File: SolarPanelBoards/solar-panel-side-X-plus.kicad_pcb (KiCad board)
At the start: 2 copper layers, 82 x 99 mm, 24 parts, among them J1 Conn_01x06, U1 OPT3001DNPT

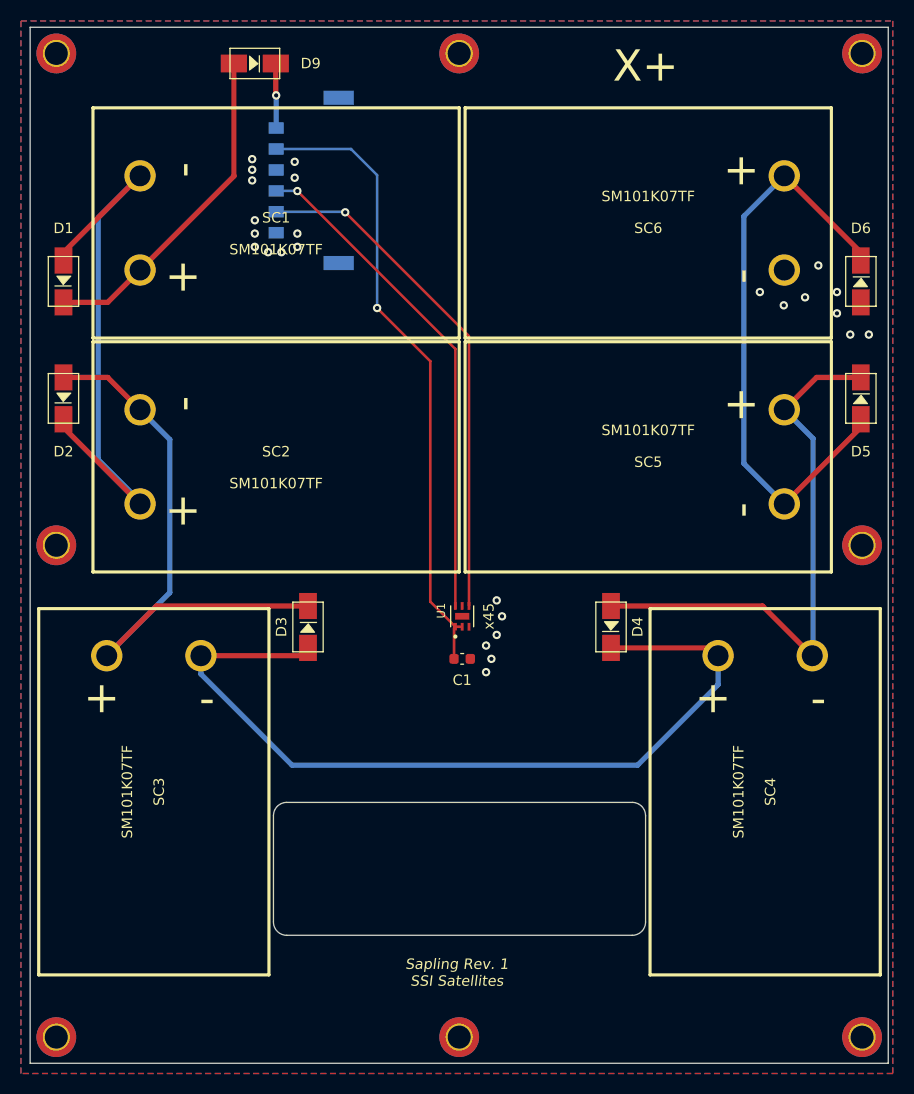
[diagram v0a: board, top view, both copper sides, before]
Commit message: Battery board and side panels ready for CAD check and review, pycubed not finished yet
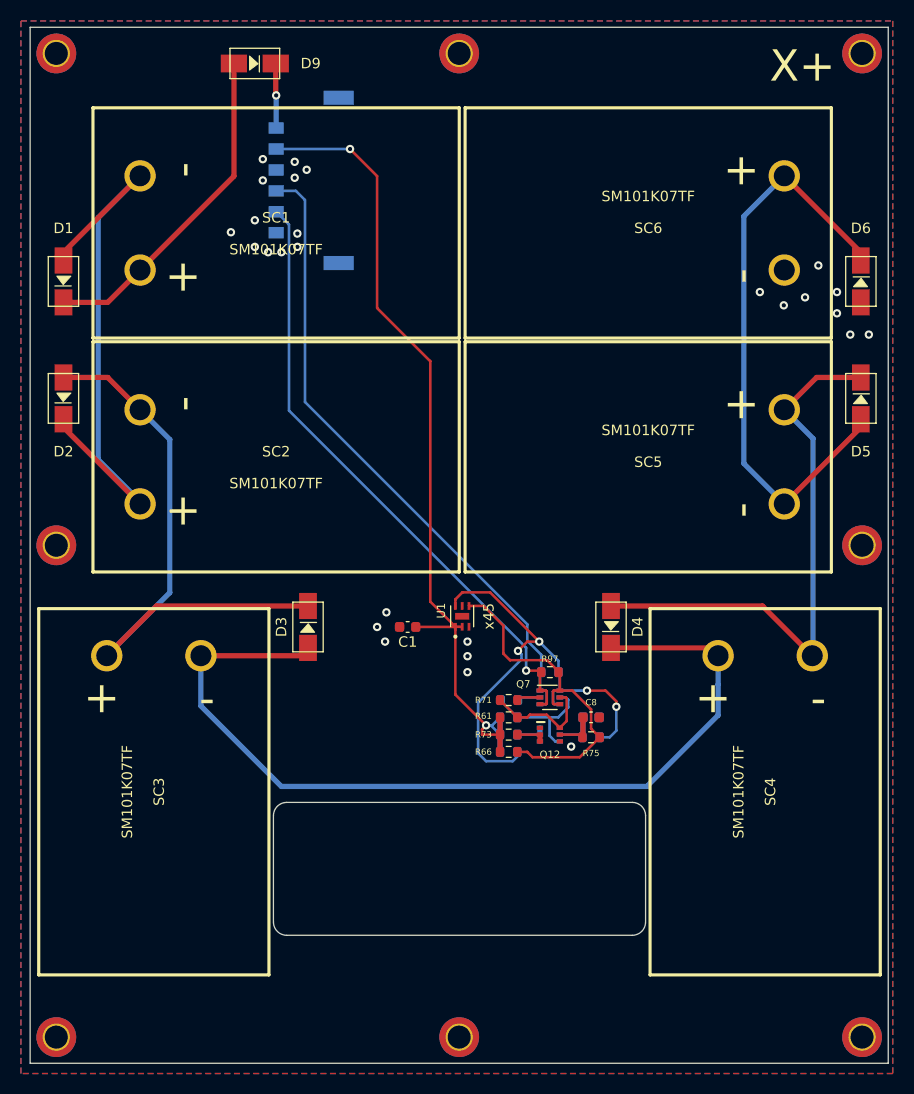
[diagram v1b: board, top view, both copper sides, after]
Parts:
- added C40: 10nF, Capacitor_SMD:C_0603_1608Metric, B.Cu at (151.0, 111.3)
- added C8: 10nF, Capacitor_SMD:C_0603_1608Metric, F.Cu at (151.0, 111.3)
- added Q12: BSS138DWQ-7, sapling:BSS138DWQ-7, F.Cu at (147.1, 112.9)
- added Q13: BSS138DWQ-7, sapling:BSS138DWQ-7, B.Cu at (147.1, 112.9)
- added Q7: MBT2222ADW1T1, Package_TO_SOT_SMD:SOT-363_SC-70-6, F.Cu at (147.1, 109.3)
- added Q8: MBT2222ADW1T1, Package_TO_SOT_SMD:SOT-363_SC-70-6, B.Cu at (147.1, 109.3)
- added R61: 10K, Resistor_SMD:R_0603_1608Metric, F.Cu at (143.1, 111.3)
- added R62: 10K, Resistor_SMD:R_0603_1608Metric, B.Cu at (143.1, 111.3)
- added R66: 10K, Resistor_SMD:R_0603_1608Metric, F.Cu at (143.1, 114.6)
- added R67: 10K, Resistor_SMD:R_0603_1608Metric, B.Cu at (143.1, 114.6)
- added R71: 680, Resistor_SMD:R_0603_1608Metric, F.Cu at (143.1, 109.6)
- added R72: 680, Resistor_SMD:R_0603_1608Metric, B.Cu at (143.2, 109.6)
- added R73: 100K, Resistor_SMD:R_0603_1608Metric, F.Cu at (143.1, 112.9)
- added R74: 100K, Resistor_SMD:R_0603_1608Metric, B.Cu at (143.1, 112.9)
- added R75: 200K, Resistor_SMD:R_0603_1608Metric, F.Cu at (151.0, 113.2)
- added R76: 200K, Resistor_SMD:R_0603_1608Metric, B.Cu at (151.0, 113.2)
- added R97: 0, Resistor_SMD:R_0603_1608Metric, F.Cu at (147.1, 106.9)
- added R98: 0, Resistor_SMD:R_0603_1608Metric, B.Cu at (147.1, 106.9)
- moved C1 6.03 mm to (133.5, 102.6), turned to 180 degrees
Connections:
- U1 pad 4: SCL -> SCL_SUN
- U1 pad 6: SDA -> SDA_SUN
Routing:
- net SDA_SUN: track 0.00 -> 48.0 mm, vias 0 -> 4
- net SCL_SUN: track 0.00 -> 32.7 mm
- net +3V3: track 60.7 -> 84.8 mm, vias 1 -> 2
- net SDA: track 47.9 -> 61.9 mm, vias 1 -> 0
- net Net-(Q13-Pad6): track 0.00 -> 12.2 mm
- net Net-(Q12-Pad6): track 0.00 -> 10.8 mm
- net SCL: track 49.1 -> 59.6 mm
- net Net-(D3-Pad2): track 81.8 -> 87.0 mm
- net Net-(C8-Pad1): track 0.00 -> 4.19 mm
- net Net-(C40-Pad1): track 0.00 -> 4.19 mm
- net Net-(Q13-Pad2): track 0.00 -> 2.81 mm
- net Net-(Q12-Pad2): track 0.00 -> 2.81 mm
- net Net-(Q7-Pad2): track 0.00 -> 2.27 mm
- net Net-(Q8-Pad2): track 0.00 -> 2.20 mm
- net GND: vias 26 -> 27
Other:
- board text removed: "Sapling Rev. 1 SSI Satellites"

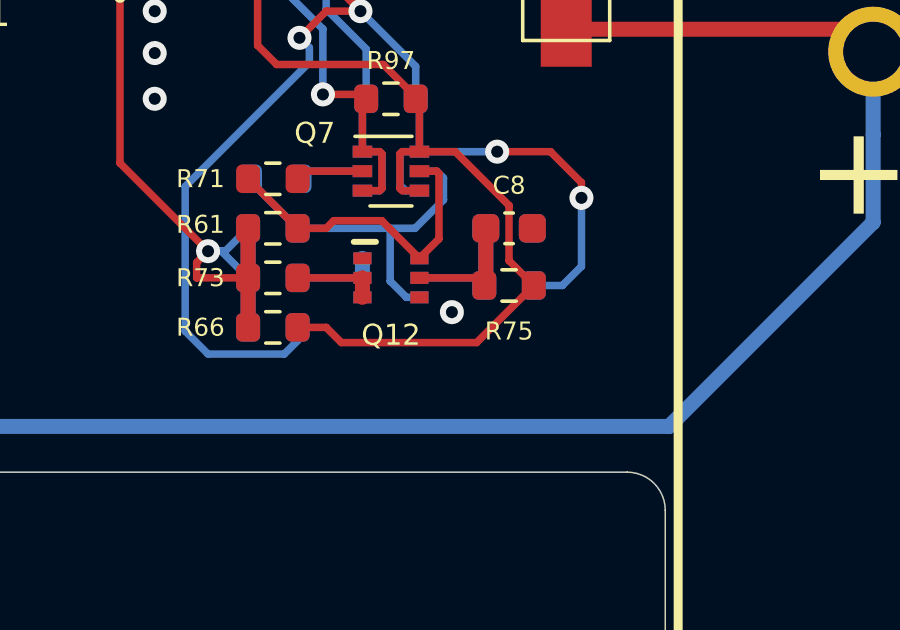
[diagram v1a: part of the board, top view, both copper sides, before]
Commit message: side panels ready except for RF trace width
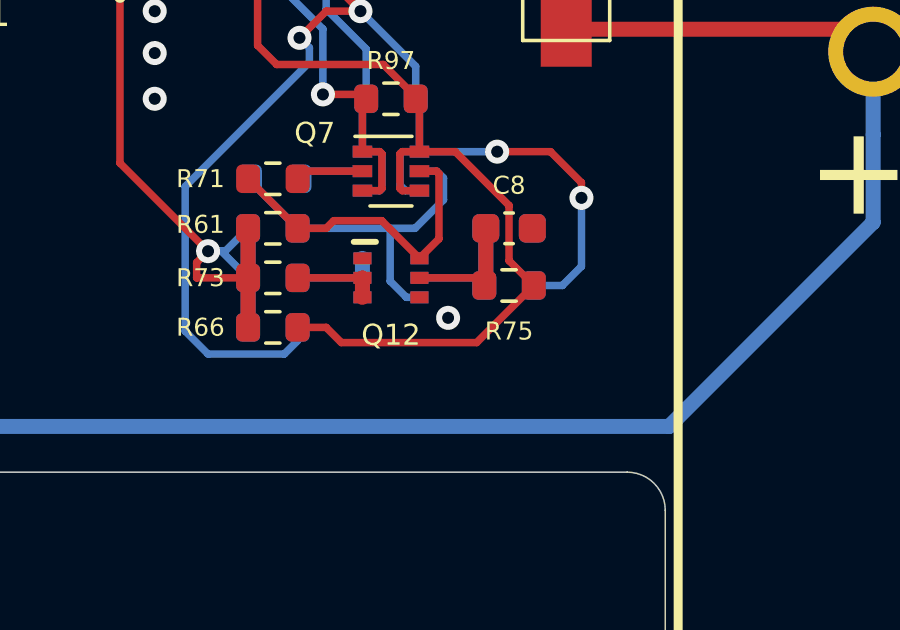
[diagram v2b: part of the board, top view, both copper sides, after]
